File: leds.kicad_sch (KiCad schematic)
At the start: 60 parts

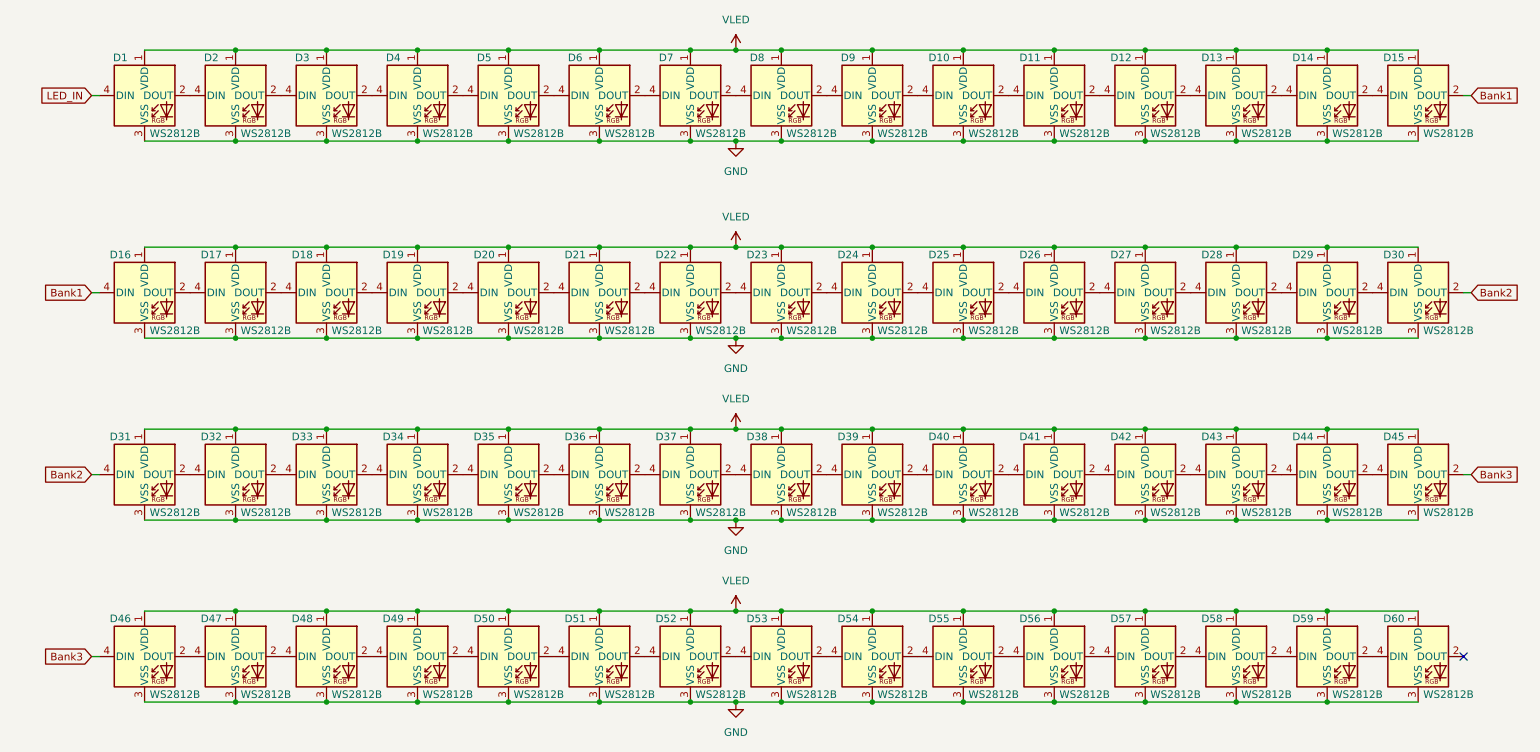
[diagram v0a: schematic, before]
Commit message: A much more reasonable architecture
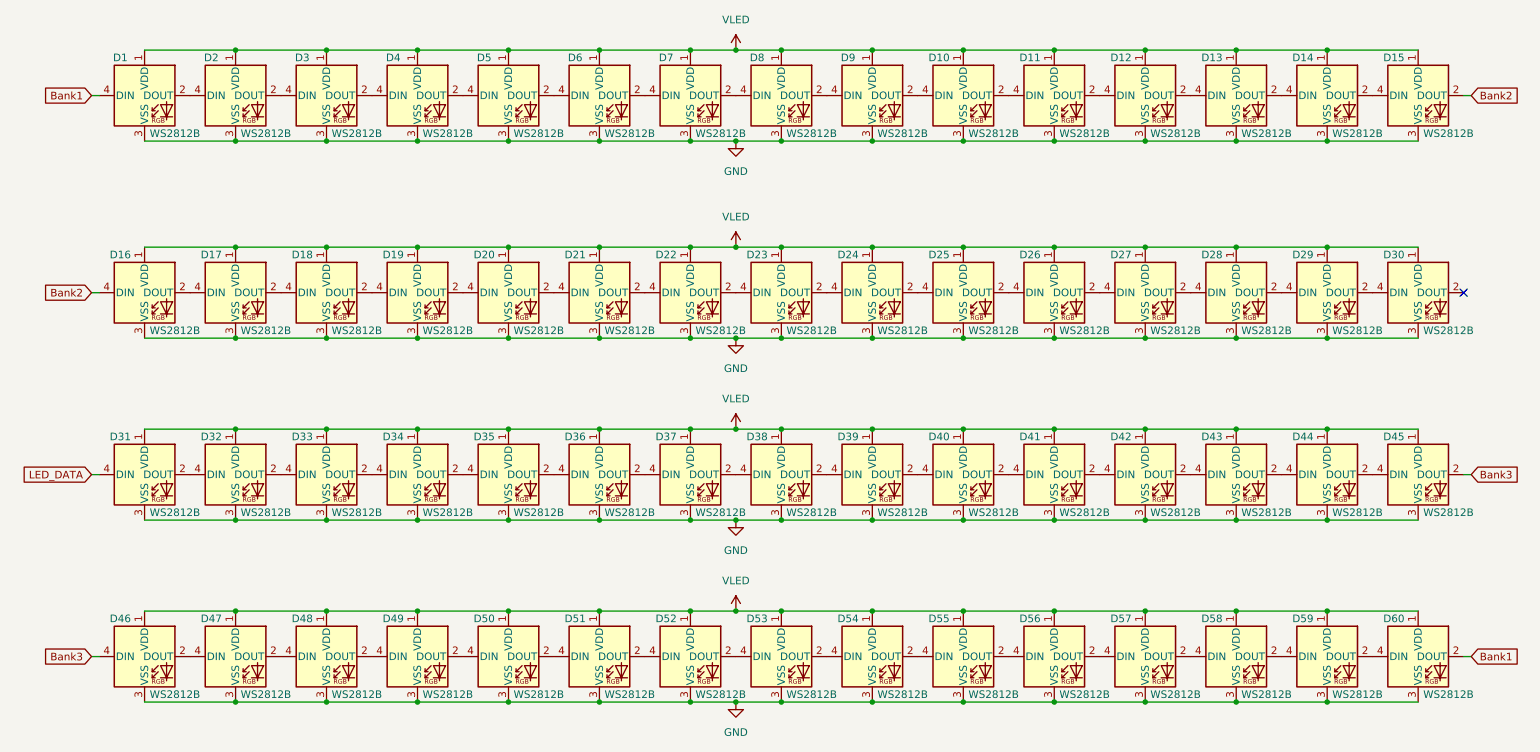
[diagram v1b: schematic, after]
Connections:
- net LED_IN is gone; now on net Bank1: D1.4 (DIN)
- net Bank1: now also D60.2 (DOUT); no longer D15.2 (DOUT), D16.4 (DIN)
- net Bank2: now also D15.2 (DOUT), D16.4 (DIN); no longer D30.2 (DOUT), D31.4 (DIN)
- new net LED_DATA: D31.4 (DIN)
